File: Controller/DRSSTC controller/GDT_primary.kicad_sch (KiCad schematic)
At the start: 20 parts, among them J401 Conn_01x01_Female, J402 Screw_Terminal_01x02, J403 Conn_01x01_Female, Q401 Q_PMOS_GDS, Q402 Q_NMOS_GDS, Q403 Q_PMOS_GDS, Q404 Q_NMOS_GDS, U401 UCC27524

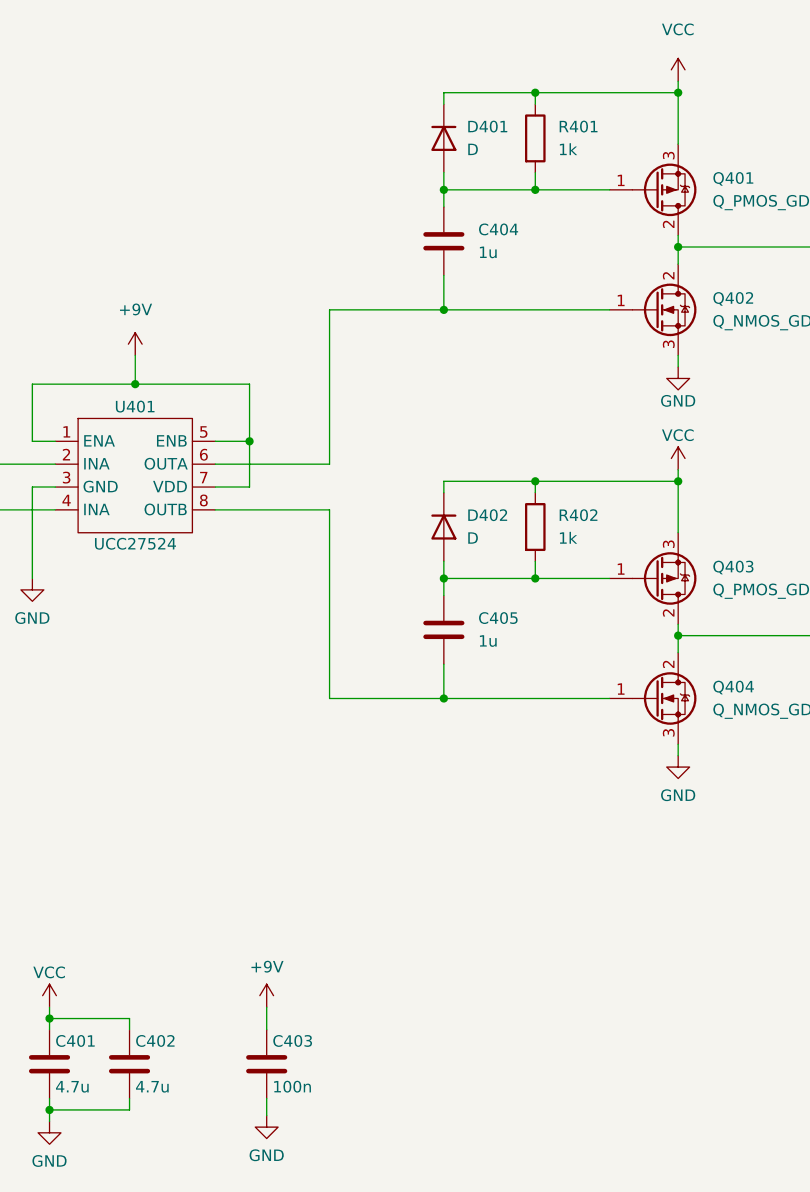
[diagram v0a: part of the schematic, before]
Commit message: 0.1V control-circuit
Next relese:
Mounting holes;
Fan header;
Better layout;
Bigger  capacitors;
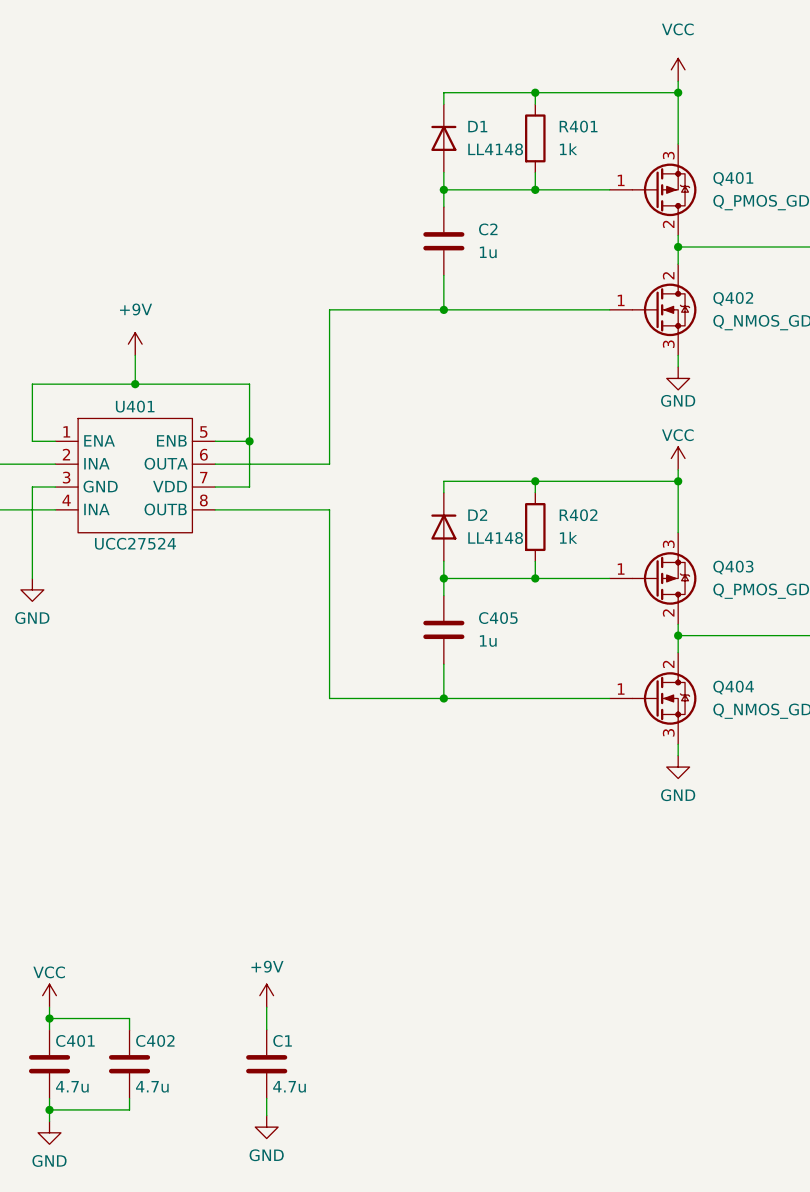
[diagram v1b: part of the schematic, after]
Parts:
- removed C403: 100n, Capacitor_SMD:C_0805_2012Metric, symbol Device:C
- removed C404: 1u, Capacitor_SMD:C_01005_0402Metric, symbol Device:C
- removed D401, D402: D, Diode_SMD:D_0805_2012Metric, symbol Device:D
- added C1: 4.7u, Capacitor_SMD:C_1206_3216Metric, symbol Device:C
- added C2: 1u, Capacitor_SMD:C_0805_2012Metric, symbol Device:C
- added D1, D2: LL4148, Diode_SMD:D_MiniMELF, symbol Diode:LL4148
- C401, C402: footprint Capacitor_THT:C_Rect_L16.5mm_W9.0mm_P15.00mm_MKT -> Capacitor_SMD:C_1206_3216Metric
- C405, C407: footprint Capacitor_SMD:C_01005_0402Metric -> Capacitor_SMD:C_0805_2012Metric
- C406: footprint Capacitor_SMD:C_1825_4564Metric -> Capacitor_SMD:C_2220_5650Metric
- J402: footprint TerminalBlock:TerminalBlock_Altech_AK300-2_P5.00mm -> TerminalBlock_Phoenix:TerminalBlock_Phoenix_PT-1,5-2-3.5-H_1x02_P3.50mm_Horizontal
- U401: footprint TestPoint:TestPoint_Loop_D2.50mm_Drill1.0mm -> Package_SO:SOIC-8_3.9x4.9mm_P1.27mm
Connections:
- net +9V: now also C1.1
- net GND: now also C1.2
- net VCC: now also D1.1 (K), D2.1 (K)
- net at Q401.1 (G), R401.2: now also C2.1, D1.2 (A)
- net at C405.1, Q403.1 (G), R402.2: now also D2.2 (A)
- net at Q402.1 (G), U401.6 (OUTA): now also C2.2
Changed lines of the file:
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@@
     )
-  )
-  (symbol (lib_id "Device:C") (at 86.995 149.86 0) (unit 1)
-    (in_bom yes) (on_board yes)
-    (property "Reference" "C403" (id 0) (at 87.63 147.32 0)
-      (effects (font (size 1.27 1.27)) (justify left))
-    )
-    (property "Value" "100n" (id 1) (at 87.63 152.4 0)
-      (effects (font (size 1.27 1.27)) (justify left))
-    )
-    (property "Footprint" "Capacitor_SMD:C_0805_2012Metric" (id 2) (at 87.9602 153.67 0)
-      (effects (font (size 1.27 1.27)) hide)
-    )
-    (property "Datasheet" "~" (id 3) (at 86.995 149.86 0)
-      (effects (font (size 1.27 1.27)) hide)
-    )
-    (pin "1")
-    (pin "2")
   )
   (symbol (lib_id "Device:Q_PMOS_GDS") (at 130.175 52.705 0) (mirror x) (unit 1)
@@
     (pin "3")
   )
-  (symbol (lib_id "Device:D") (at 106.68 46.99 270) (unit 1)
-    (in_bom yes) (on_board yes) (fields_autoplaced)
-    (property "Reference" "D401" (id 0) (at 109.22 45.7199 90)
-      (effects (font (size 1.27 1.27)) (justify left))
-    )
-    (property "Value" "D" (id 1) (at 109.22 48.2599 90)
-      (effects (font (size 1.27 1.27)) (justify left))
-    )
-    (property "Footprint" "Diode_SMD:D_0805_2012Metric" (id 2) (at 106.68 46.99 0)
-      (effects (font (size 1.27 1.27)) hide)
-    )
-    (property "Datasheet" "~" (id 3) (at 106.68 46.99 0)
-      (effects (font (size 1.27 1.27)) hide)
-    )
-    (pin "1")
-    (pin "2")
-  )
   (symbol (lib_id "Device:C") (at 71.755 149.86 0) (unit 1)
     (in_bom yes) (on_board yes)
@@
       (effects (font (size 1.27 1.27)) (justify left))
     )
-    (property "Footprint" "Capacitor_THT:C_Rect_L16.5mm_W9.0mm_P15.00mm_MKT" (id 2) (at 72.7202 153.67 0)
+    (property "Footprint" "Capacitor_SMD:C_1206_3216Metric" (id 2) (at 72.7202 153.67 0)
       (effects (font (size 1.27 1.27)) hide)
     )
@@
     (pin "2")
   )
+  (symbol (lib_id "Diode:LL4148") (at 106.68 90.17 270) (unit 1)
+    (in_bom yes) (on_board yes) (fields_autoplaced)
+    (property "Reference" "D2" (id 0) (at 109.22 88.8999 90)
+      (effects (font (size 1.27 1.27)) (justify left))
+    )
+    (property "Value" "LL4148" (id 1) (at 109.22 91.4399 90)
+      (effects (font (size 1.27 1.27)) (justify left))
+    )
+    (property "Footprint" "Diode_SMD:D_MiniMELF" (id 2) (at 102.235 90.17 0)
+      (effects (font (size 1.27 1.27)) hide)
+    )
+    (property "Datasheet" "http://www.vishay.com/docs/85557/ll4148.pdf" (id 3) (at 106.68 90.17 0)
+      (effects (font (size 1.27 1.27)) hide)
+    )
+    (pin "1")
+    (pin "2")
+  )
   (symbol (lib_id "Device:C") (at 106.68 101.6 0) (unit 1)
     (in_bom yes) (on_board yes) (fields_autoplaced)
@@
       (effects (font (size 1.27 1.27)) (justify left))
     )
-    (property "Footprint" "Capacitor_SMD:C_01005_0402Metric" (id 2) (at 107.6452 105.41 0)
+    (property "Footprint" "Capacitor_SMD:C_0805_2012Metric" (id 2) (at 107.6452 105.41 0)
       (effects (font (size 1.27 1.27)) hide)
     )
@@
     (pin "2")
     (pin "3")
-  )
-  (symbol (lib_id "Device:C") (at 106.68 58.42 0) (unit 1)
-    (in_bom yes) (on_board yes) (fields_autoplaced)
-    (property "Reference" "C404" (id 0) (at 110.49 57.1499 0)
-      (effects (font (size 1.27 1.27)) (justify left))
-    )
-    (property "Value" "1u" (id 1) (at 110.49 59.6899 0)
-      (effects (font (size 1.27 1.27)) (justify left))
-    )
-    (property "Footprint" "Capacitor_SMD:C_01005_0402Metric" (id 2) (at 107.6452 62.23 0)
-      (effects (font (size 1.27 1.27)) hide)
-    )
-    (property "Datasheet" "~" (id 3) (at 106.68 58.42 0)
-      (effects (font (size 1.27 1.27)) hide)
-    )
-    (pin "1")
-    (pin "2")
   )
   (symbol (lib_id "Device:C") (at 161.29 59.055 90) (unit 1)
@@
     (property "Reference" "C406" (id 0) (at 161.29 55.88 90))
     (property "Value" "2.2u" (id 1) (at 161.29 62.23 90))
-    (property "Footprint" "Capacitor_SMD:C_1825_4564Metric" (id 2) (at 165.1 58.0898 0)
+    (property "Footprint" "Capacitor_SMD:C_2220_5650Metric" (id 2) (at 165.1 58.0898 0)
       (effects (font (size 1.27 1.27)) hide)
     )
@@
       (effects (font (size 1.27 1.27)) (justify left))
     )
-    (property "Footprint" "TerminalBlock:TerminalBlock_Altech_AK300-2_P5.00mm" (id 2) (at 191.135 76.835 0)
+    (property "Footprint" "TerminalBlock_Phoenix:TerminalBlock_Phoenix_PT-1,5-2-3.5-H_1x02_P3.50mm_Horizontal" (id 2) (at 191.135 76.835 0)
       (effects (font (size 1.27 1.27)) hide)
     )
@@
       (effects (font (size 1.27 1.27)) (justify left))
     )
-    (property "Footprint" "Capacitor_THT:C_Rect_L16.5mm_W9.0mm_P15.00mm_MKT" (id 2) (at 63.8302 153.67 0)
+    (property "Footprint" "Capacitor_SMD:C_1206_3216Metric" (id 2) (at 63.8302 153.67 0)
       (effects (font (size 1.27 1.27)) hide)
     )
@@
     (property "Reference" "U401" (id 0) (at 72.39 76.835 0))
     (property "Value" "UCC27524" (id 1) (at 72.39 92.075 0))
-    (property "Footprint" "TestPoint:TestPoint_Loop_D2.50mm_Drill1.0mm" (id 2) (at 69.85 85.725 0)
-      (effects (font (size 1.27 1.27)) hide)
-    )
-    (property "Datasheet" "" (id 3) (at 69.85 85.725 0)
+    (property "Footprint" "Package_SO:SOIC-8_3.9x4.9mm_P1.27mm" (id 2) (at 72.39 93.98 0)
+      (effects (font (size 1.27 1.27)) hide)
+    )
+    (property "Datasheet" "https://datasheet.lcsc.com/lcsc/1912111437_Texas-Instruments-UCC27524DR_C465729.pdf" (id 3) (at 69.85 85.725 0)
       (effects (font (size 1.27 1.27)) hide)
     )
@@
     (pin "8")
   )
-  (symbol (lib_id "Device:D") (at 106.68 90.17 270) (unit 1)
-    (in_bom yes) (on_board yes) (fields_autoplaced)
-    (property "Reference" "D402" (id 0) (at 109.22 88.8999 90)
-      (effects (font (size 1.27 1.27)) (justify left))
-    )
-    (property "Value" "D" (id 1) (at 109.22 91.4399 90)
-      (effects (font (size 1.27 1.27)) (justify left))
-    )
-    (property "Footprint" "Diode_SMD:D_0805_2012Metric" (id 2) (at 106.68 90.17 0)
-      (effects (font (size 1.27 1.27)) hide)
-    )
-    (property "Datasheet" "~" (id 3) (at 106.68 90.17 0)
+  (symbol (lib_id "Device:C") (at 106.68 58.42 0) (unit 1)
+    (in_bom yes) (on_board yes) (fields_autoplaced)
+    (property "Reference" "C2" (id 0) (at 110.49 57.1499 0)
+      (effects (font (size 1.27 1.27)) (justify left))
+    )
+    (property "Value" "1u" (id 1) (at 110.49 59.6899 0)
+      (effects (font (size 1.27 1.27)) (justify left))
+    )
+    (property "Footprint" "Capacitor_SMD:C_0805_2012Metric" (id 2) (at 107.6452 62.23 0)
+      (effects (font (size 1.27 1.27)) hide)
+    )
+    (property "Datasheet" "~" (id 3) (at 106.68 58.42 0)
+      (effects (font (size 1.27 1.27)) hide)
+    )
+    (pin "1")
+    (pin "2")
+  )
+  (symbol (lib_id "Diode:LL4148") (at 106.68 46.99 270) (unit 1)
+    (in_bom yes) (on_board yes) (fields_autoplaced)
+    (property "Reference" "D1" (id 0) (at 109.22 45.7199 90)
+      (effects (font (size 1.27 1.27)) (justify left))
+    )
+    (property "Value" "LL4148" (id 1) (at 109.22 48.2599 90)
+      (effects (font (size 1.27 1.27)) (justify left))
+    )
+    (property "Footprint" "Diode_SMD:D_MiniMELF" (id 2) (at 102.235 46.99 0)
+      (effects (font (size 1.27 1.27)) hide)
+    )
+    (property "Datasheet" "http://www.vishay.com/docs/85557/ll4148.pdf" (id 3) (at 106.68 46.99 0)
       (effects (font (size 1.27 1.27)) hide)
     )
@@
     (pin "1")
   )
+  (symbol (lib_id "Device:C") (at 86.995 149.86 0) (unit 1)
+    (in_bom yes) (on_board yes)
+    (property "Reference" "C1" (id 0) (at 87.63 147.32 0)
+      (effects (font (size 1.27 1.27)) (justify left))
+    )
+    (property "Value" "4.7u" (id 1) (at 87.63 152.4 0)
+      (effects (font (size 1.27 1.27)) (justify left))
+    )
+    (property "Footprint" "Capacitor_SMD:C_1206_3216Metric" (id 2) (at 87.9602 153.67 0)
+      (effects (font (size 1.27 1.27)) hide)
+    )
+    (property "Datasheet" "~" (id 3) (at 86.995 149.86 0)
+      (effects (font (size 1.27 1.27)) hide)
+    )
+    (pin "1")
+    (pin "2")
+  )
   (symbol (lib_id "Device:C") (at 165.1 53.975 90) (unit 1)
     (in_bom yes) (on_board yes) (fields_autoplaced)
     (property "Reference" "C407" (id 0) (at 165.1 46.99 90))
     (property "Value" "1u" (id 1) (at 165.1 49.53 90))
-    (property "Footprint" "Capacitor_SMD:C_01005_0402Metric" (id 2) (at 168.91 53.0098 0)
-      (effects (font (size 1.27 1.27)) hide)
-    )
+    (property "Footprint" "Capacitor_SMD:C_0805_2012Metric" (id 2) (at 168.91 53.0098 0)
+      (effects (font (size 1.27 1.27)) hide)
+    )

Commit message: V0.2a
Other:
- company: (none) -> Politehnika
- title: (none) -> DRSSTC controller
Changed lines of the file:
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@@
 (kicad_sch (version 20211123) (generator eeschema)
   (paper "A4")
+  (title_block
+    (title "DRSSTC controller")
+    (date "2023-03-07")
+    (rev "0.2")
+    (company "Politehnika")
+  )
   (junction (at 116.84 85.09) (diameter 0) (color 0 0 0 0)
   )

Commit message: V0.2c
Added stl files
PCB update
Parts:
- Q201: renamed from Q401; footprint Package_TO_SOT_SMD:TO-252-3_TabPin2 -> Package_TO_SOT_SMD:TO-252-2
- Q202: renamed from Q402; footprint Package_TO_SOT_SMD:TO-252-3_TabPin2 -> Package_TO_SOT_SMD:TO-252-2
- Q203: renamed from Q403; footprint Package_TO_SOT_SMD:TO-252-3_TabPin2 -> Package_TO_SOT_SMD:TO-252-2
- Q204: renamed from Q404; footprint Package_TO_SOT_SMD:TO-252-3_TabPin2 -> Package_TO_SOT_SMD:TO-252-2
- renumbered C401 to C201, C402 to C202, C1 to C203, C2 to C204, C405 to C205, C406 to C206, C407 to C207, D1 to D201, D2 to D202, J401 to J201, J402 to J202, J403 to J203, R401 to R201, R402 to R202, R403 to R203, U401 to U201

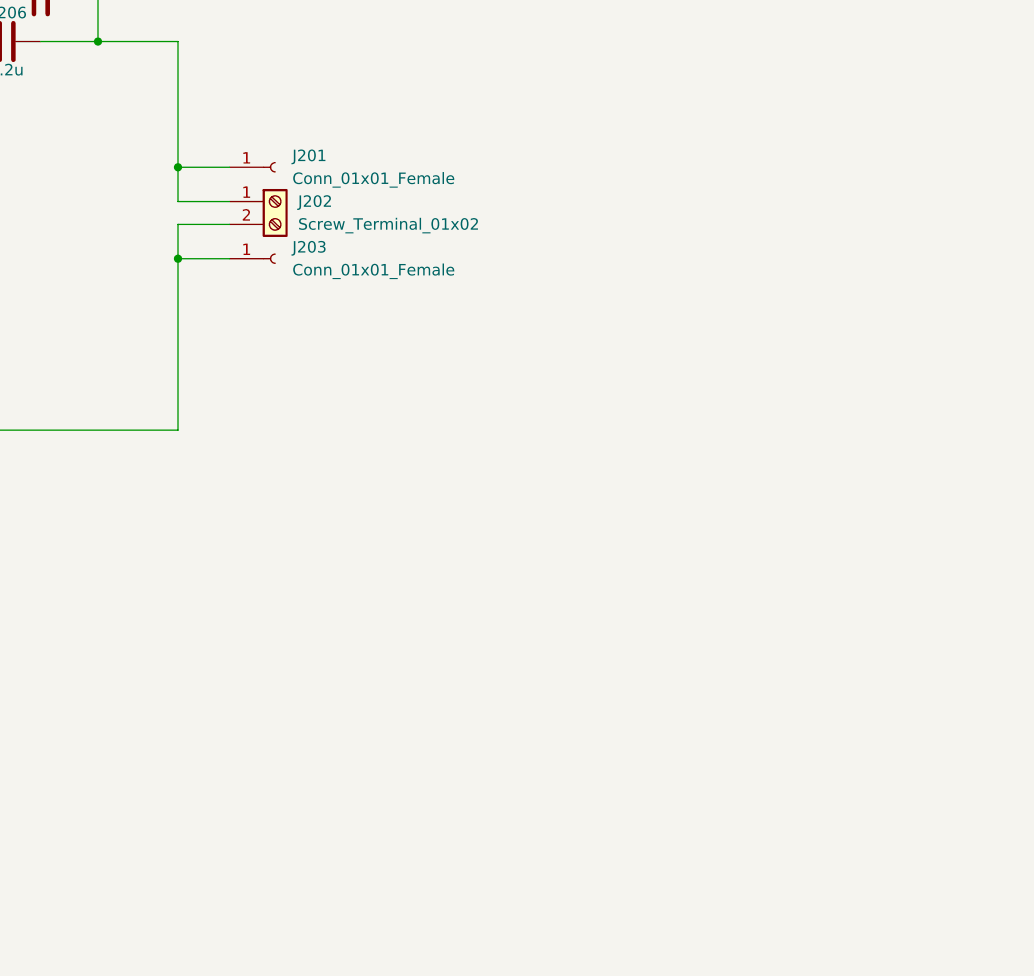
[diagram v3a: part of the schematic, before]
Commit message: Updated circuit
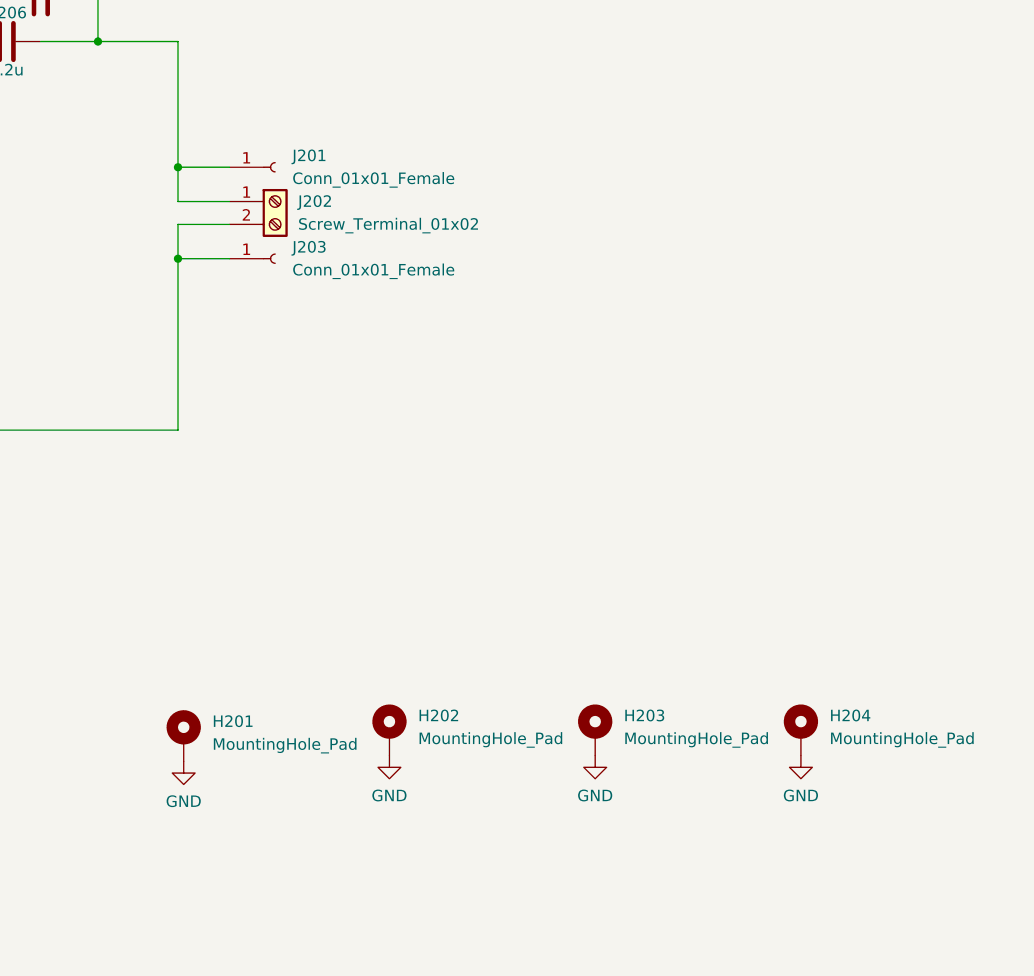
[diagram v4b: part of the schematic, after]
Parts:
- added H201, H202, H203, H204: MountingHole_Pad, MountingHole:MountingHole_3.2mm_M3_Pad_Via, symbol Mechanical:MountingHole_Pad
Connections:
- net GND: now also H201.1, H202.1, H203.1, H204.1
